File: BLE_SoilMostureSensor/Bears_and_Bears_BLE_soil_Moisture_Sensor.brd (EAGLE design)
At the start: 35.6 x 76.2 mm, 51 parts, among them Q1 2N3904, U2 EFR32BG13, X1 20317

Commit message: fixing antenna
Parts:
- removed FID1, FID2: FIDUCIAL"", microbuilder:FIDUCIAL_1MM
- removed TP6: TEST-POINT3, SparkFun-Connectors:PAD.03X.03
- added R11: 4.7k, SparkFun-Resistors:0603
- added Y1: (no value), Crystal_SMD_1.2x0.6:CRYSTAL_1.2X0.6
- L1: value L100 -> 33nH/±5%/500mA
- L2, L4: value 1.9NH -> 3.9NH
- U$3: value 38.4MHZ_CRYSTAL -> (none)
- moved U$3 88.2 mm to (12.5, 52.2), turned to 180 degrees
- moved U2 86.3 mm to (17.0, 56.5)
- moved TP4 85.6 mm to (8.26, 66.5)
- moved TP2 84.4 mm to (8.26, 68.4)
- moved TP5 77.7 mm to (22.5, 53.5)
- moved TP3 70.9 mm to (18.1, 51.0)
- moved R10 67.8 mm to (23.0, 51.8), turned to 180 degrees
- moved TP1 65.2 mm to (20.3, 47.3)
- moved R2 42.7 mm to (1.91, 48.3)
- moved FB1 38.7 mm to (8.57, 53.3)
- moved C11 34.3 mm to (8.57, 55.2), turned to 180 degrees
- moved L4 33.7 mm to (13.0, 69.1), turned to 180 degrees
- moved C12 32.8 mm to (8.57, 56.8), turned to 180 degrees
- moved C10 27.4 mm to (20.3, 69.2), turned to 180 degrees
- moved R9 27.0 mm to (16.2, 69.1), turned to 180 degrees
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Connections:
- removed net N$52: X1.9
- removed net N$7: TP6.P$1
- removed net N$8: TP5.P$1
- new net GND_DETECT: R11.1, U2.23, X1.9
- new net HFXTAL_N: U$3.1, U2.10
- new net HFXTAL_P: U$3.3, U2.11
- new net LFXTAL_N: U2.35, Y1.P$1
- new net LFXTAL_P: U2.36, Y1.P$2
- new net N$10: U2.6
- new net N$11: U2.7
- new net N$12: U2.8
- new net N$16: U2.26
- new net N$17: U2.27
- new net N$18: U2.28
- new net N$19: U2.29
- new net N$2: U2.14, U2.15, U2.37, U2.GND
- new net N$20: U2.30
- new net N$9: U2.5
- net DECOUPLE: now also U2.41; no longer U2.42
- net GND: now also U$3.GND, U$3.GND2, U2.16
- net IOP: now also U2.17
- net PAVDD: no longer FB2.1
- net RADIO_RESET: now also U2.12
- net RFVDD: now also U2.9
- net SCL: now also U2.47
- net SDA: now also U2.48
- net SENSOR_ENABLE: now also TP5.P$1, U2.24
- net SIG: now also U2.25
- net SOIL_MOIST_PWR: now also U2.20
- net TCK: now also U2.1
- net TDI: now also U2.4
- net TDO: now also U2.3
- net TMS: now also U2.2
- net VDCDC: no longer U2.41
- net VDD: now also FB2.1, R11.2; no longer C4.1, C5.1, C6.1, L1.1, U2.38, U2.39
- net VREGSW: now also U2.38
- net V_BATT: now also C4.1, C5.1, C6.1, L1.1, U2.39, U2.42
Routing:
- net V_BATT: track 0.00 -> 26.6 mm, vias 0 -> 2
- net N$3: track 0.00 -> 17.9 mm
- net PROBE1: track 0.00 -> 11.2 mm
- net VDCDC: track 0.00 -> 10.9 mm
- net SCL: track 0.00 -> 10.6 mm
- net SDA: track 0.00 -> 8.38 mm
- net TCK: track 0.00 -> 8.29 mm
- net VREGSW: track 0.00 -> 8.19 mm, vias 0 -> 2
- net AVDD: track 0.00 -> 7.01 mm
- net PAVDD: track 0.00 -> 6.60 mm
- net SDA_IN: track 0.00 -> 6.46 mm
- net RFVDD: track 0.00 -> 5.78 mm
- net SCL_IN: track 0.00 -> 4.02 mm
- net LFXTAL_N: track 0.00 -> 3.42 mm
- net LFXTAL_P: track 0.00 -> 3.37 mm
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- added copper zone on layer 1, net GND
- added copper zone on layer 16, net GND
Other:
- board size 35.6 x 76.2 mm -> 33.6 x 76.2 mm

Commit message: first prototype
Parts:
- removed STANDOFF1, STANDOFF2: STAND-OFF, SparkFun-Electromechanical:STAND-OFF
- added U$4: IMAGES#JPG, images#jpg(2):IMAGES#JPG
- E1: value ANTENNA-GROUNDEDTRACE-15.2MM -> ANTENNA-GROUNDEDTRACE-25.7MM; device SparkFun-RF:TRACE_ANTENNA_2.4GHZ_15.2MM -> SparkFun-RF:TRACE_ANTENNA_2.4GHZ_25.7MM
- moved FRAME2 107.9 mm to (59.1, -8.57)
- moved C6 62.5 mm to (64.4, 62.8), turned to 0 degrees
- moved R2 48.6 mm to (50.5, 47.3), turned to 0 degrees
- moved C9 44.8 mm to (56.2, 60.6), turned to 90 degrees
- moved U$2 43.2 mm to (45.4, 62.9)
- moved E1 40.8 mm to (53.3, 71.6)
- moved C2 40.7 mm to (70.0, 60.3)
- moved C3 40.7 mm to (70.0, 58.4)
- moved L1 40.7 mm to (70.0, 54.9)
- moved R7 40.7 mm to (70.0, 56.7)
- moved X1 40.4 mm to (43.0, 50.8)
- moved C12 40.3 mm to (48.9, 56.8)
- moved Y1 40.1 mm to (62.2, 56.4), turned to 90 degrees
- moved Q1 40.0 mm to (69.4, 49.2)
- moved R1 40.0 mm to (69.4, 52.1)
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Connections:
- removed net N$2: U2.14, U2.15, U2.37, U2.GND
- net GND: now also E1.GND2, U2.14, U2.15, U2.37, U2.GND
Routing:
- net VDD: track 2.45 -> 87.9 mm, vias 0 -> 4
- net PAVDD: track 6.60 -> 50.9 mm, vias 0 -> 2
- net SENSOR_ENABLE: track 0.00 -> 31.7 mm, vias 0 -> 2
- net V_BATT: track 26.6 -> 57.3 mm, vias 2 -> 7
- net GND_DETECT: track 0.00 -> 25.6 mm, vias 0 -> 2
- net AVDD: track 7.01 -> 29.4 mm, vias 0 -> 2
- net SOIL_MOIST_PWR: track 0.00 -> 20.9 mm
- net VDCDC: track 10.9 -> 30.3 mm, vias 0 -> 3
- net GND: track 0.00 -> 17.0 mm, vias 0 -> 17
- net PROBE2: track 0.00 -> 16.1 mm
- net RFVDD: track 5.78 -> 21.4 mm, vias 0 -> 3
- net SDA: track 8.38 -> 22.6 mm, vias 0 -> 2
- net SCL_IN: track 4.02 -> 18.1 mm, vias 0 -> 2
- net SIG: track 1.97 -> 14.2 mm
- net TDI: track 0.00 -> 10.3 mm, vias 0 -> 2
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- added copper zone on layer 2, net GND
- added copper zone on layer 15, net V_BATT
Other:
- board size 33.6 x 76.2 mm -> 33.6 x 78.4 mm
- board text added: "1"
- board text added: "2"
- board text added: "3"
- board text added: "4"
- board text added: "5"
- board text added: "BLE SOIL MOISTURE SENSOR"
- board text added: "LIGHT"
- board text added: "TEMP"

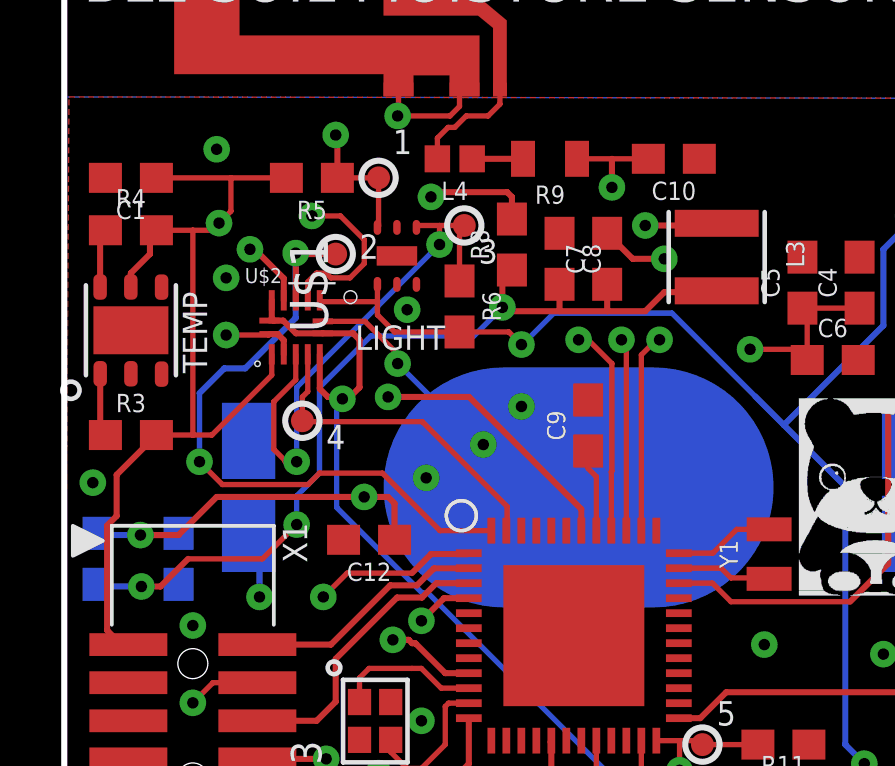
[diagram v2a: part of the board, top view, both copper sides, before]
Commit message: updating sch - 12c, power
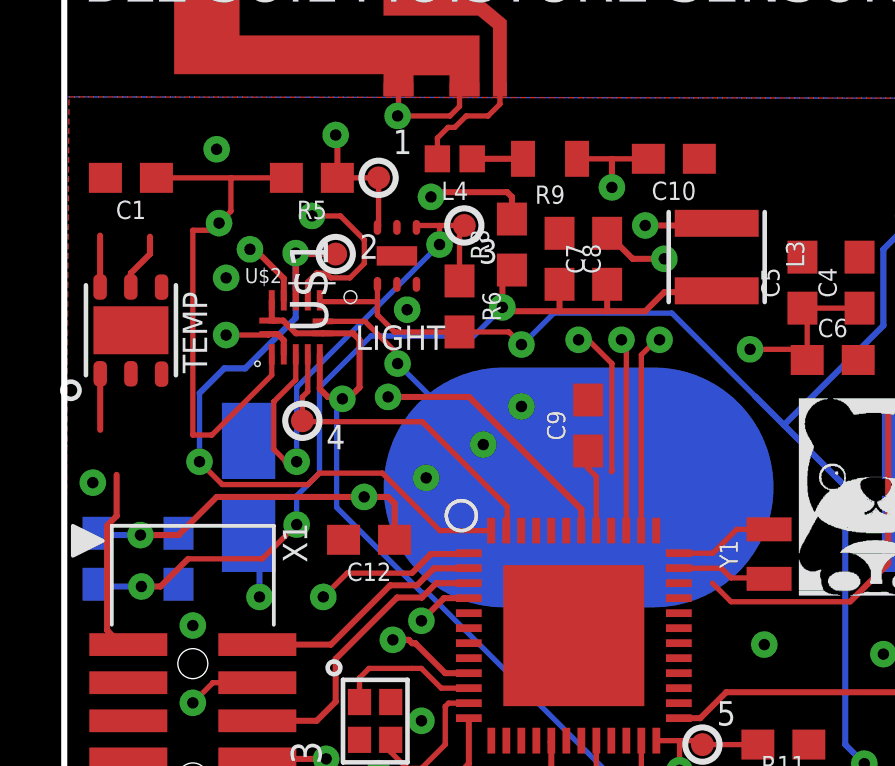
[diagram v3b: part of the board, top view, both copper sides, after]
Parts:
- removed R3, R4: 10k, SparkFun-Resistors:0603
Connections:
- removed net N$1: R4.1, U1.SCL
- removed net N$4: R3.1, U1.SDA
- new net DVDD: U2.40
- net AVDD: now also U2.34; no longer U2.40
- net PAVDD: now also U2.18; no longer U2.34
- net SCL_IN: now also U1.SCL
- net SDA_IN: now also U1.SDA
- net VDD: no longer R3.2, R4.2
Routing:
- net VDD: track 87.9 -> 83.2 mm
- net N$4: track 2.11 -> 0.00 mm
- net AVDD: track 29.4 -> 27.5 mm
- net N$1: track 1.97 -> 0.00 mm
- net SDA_IN: track 12.8 -> 14.6 mm
- net SCL_IN: track 18.1 -> 19.8 mm
- net PAVDD: track 50.9 -> 49.8 mm
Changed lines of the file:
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@@
 <attribute name="PROD_ID" value="CAP-00810" x="40.9575" y="68.8975" size="1.778" layer="27" rot="R180" display="off"/>
-</element>
-<element name="R3" library="SparkFun-Resistors" package="0603" value="10k" x="40.9575" y="60.325">
-<attribute name="PROD_ID" value="RES-00824" x="40.9575" y="60.325" size="1.778" layer="27" display="off"/>
-</element>
-<element name="R4" library="SparkFun-Resistors" package="0603" value="10k" x="40.9575" y="67.15125">
-<attribute name="PROD_ID" value="RES-00824" x="40.9575" y="67.15125" size="1.778" layer="27" display="off"/>
 </element>
 <element name="U$1" library="ALS_OPT3001" package="6PIN_USON" value="" x="50.8" y="65.24625" rot="R90"/>
@@
 <wire x1="41.275" y1="45.4025" x2="41.275" y2="38.4175" width="0.1778" layer="1"/>
 </signal>
-<signal name="N$1">
-<contactref element="U1" pad="SCL"/>
-<contactref element="R4" pad="1"/>
-<wire x1="39.9305" y1="65.2595" x2="39.9305" y2="66.97425" width="0.2032" layer="1"/>
-<wire x1="39.9305" y1="66.97425" x2="40.1075" y2="67.15125" width="0.2032" layer="1"/>
-</signal>
-<signal name="N$4">
-<contactref element="U1" pad="SDA"/>
-<contactref element="R3" pad="1"/>
-<wire x1="39.9335" y1="62.3675" x2="39.9335" y2="60.499" width="0.2032" layer="1"/>
-<wire x1="39.9335" y1="60.499" x2="40.1075" y2="60.325" width="0.2032" layer="1"/>
-</signal>
 <signal name="SCL_IN">
 <contactref element="U$2" pad="NO2"/>
@@
 <via x="46.482" y="59.436" extent="1-16" drill="0.381"/>
 <via x="51.2445" y="66.675" extent="1-16" drill="0.381"/>
+<contactref element="U1" pad="SCL"/>
+<wire x1="39.9305" y1="65.2595" x2="39.9305" y2="66.97425" width="0.2032" layer="1"/>
+<wire x1="39.9305" y1="65.2595" x2="46.4525" y2="63.015" width="0" layer="19" extent="1-1"/>
 </signal>
 <signal name="SCL">
@@
 <contactref element="U$2" pad="NO3"/>
 <contactref element="C1" pad="1"/>
-<contactref element="R3" pad="2"/>
-<contactref element="R4" pad="2"/>
 <contactref element="U1" pad="VCC"/>
 <contactref element="U$1" pad="1"/>
@@
 <wire x1="40.9545" y1="65.2615" x2="40.9545" y2="65.7195" width="0.2032" layer="1"/>
 <wire x1="41.5925" y1="66.3575" x2="40.9545" y2="65.7195" width="0.2032" layer="1"/>
-<wire x1="41.8075" y1="67.15125" x2="41.5925" y2="66.93625" width="0.2032" layer="1"/>
 <wire x1="41.5925" y1="66.93625" x2="41.5925" y2="66.3575" width="0.2032" layer="1"/>
 <wire x1="41.8075" y1="68.8975" x2="44.29125" y2="68.8975" width="0.1778" layer="1"/>
 <wire x1="44.29125" y1="68.8975" x2="46.14" y2="68.8975" width="0.1778" layer="1"/>
-<wire x1="41.8075" y1="67.15125" x2="43.02125" y2="67.15125" width="0.1778" layer="1"/>
 <wire x1="43.02125" y1="67.15125" x2="43.65625" y2="67.15125" width="0.1778" layer="1"/>
 <wire x1="44.29125" y1="67.78625" x2="44.29125" y2="68.8975" width="0.1778" layer="1"/>
@@
 <wire x1="45.6525" y1="62.32125" x2="43.65625" y2="60.325" width="0.1778" layer="1"/>
 <wire x1="43.65625" y1="60.325" x2="43.02125" y2="60.325" width="0.1778" layer="1"/>
-<wire x1="43.02125" y1="60.325" x2="41.8075" y2="60.325" width="0.1778" layer="1"/>
 <wire x1="43.02125" y1="67.15125" x2="43.02125" y2="60.325" width="0.1778" layer="1"/>
-<wire x1="41.8075" y1="60.325" x2="41.75125" y2="60.26875" width="0.1778" layer="1"/>
 <wire x1="40.64" y1="53.34" x2="40.87125" y2="53.34" width="0.1778" layer="1"/>
 <wire x1="58.9915" y1="64.389" x2="61.769625" y2="61.610875" width="0.1778" layer="16"/>
@@
 <wire x1="66.04" y1="63.97625" x2="62.722125" y2="60.658375" width="0.2032" layer="16"/>
 <wire x1="66.04" y1="66.51625" x2="66.04" y2="63.97625" width="0.2032" layer="16"/>
-<wire x1="41.8075" y1="60.325" x2="40.48125" y2="58.99875" width="0.2032" layer="1"/>
 <wire x1="40.48125" y1="57.62625" x2="40.16375" y2="57.30875" width="0.2032" layer="1"/>
 <wire x1="40.16375" y1="57.30875" x2="40.16375" y2="53.81625" width="0.2032" layer="1"/>
@@
 <wire x1="53.975" y1="63.34125" x2="54.00675" y2="63.34125" width="0.1778" layer="16"/>
 <wire x1="54.00675" y1="63.34125" x2="55.0545" y2="64.389" width="0.1778" layer="16"/>
+<wire x1="43.02125" y1="67.15125" x2="41.5925" y2="66.93625" width="0" layer="19" extent="1-1"/>
+<wire x1="40.48125" y1="58.99875" x2="43.02125" y2="60.325" width="0" layer="19" extent="1-1"/>
 </signal>
 <signal name="SDA_IN">
@@
 <wire x1="47.84" y1="68.8975" x2="47.84" y2="70.27" width="0.2032" layer="1"/>
 <wire x1="47.84" y1="70.27" x2="47.78375" y2="70.32625" width="0.2032" layer="1"/>
+<contactref element="U1" pad="SDA"/>
+<wire x1="39.9335" y1="62.3675" x2="39.9335" y2="60.499" width="0.2032" layer="1"/>
+<wire x1="39.9335" y1="62.3675" x2="44.92625" y2="66.51625" width="0" layer="19" extent="1-1"/>
 </signal>
 <signal name="SDA">
@@
 <contactref element="C3" pad="1"/>
 <contactref element="C2" pad="2"/>
-<contactref element="U2" pad="40"/>
 <wire x1="69.15875" y1="56.67375" x2="68.10375" y2="56.67375" width="0.1778" layer="1"/>
 <wire x1="68.10375" y1="56.67375" x2="67.945" y2="56.8325" width="0.1778" layer="1"/>
@@
 <wire x1="67.945" y1="58.42" x2="67.945" y2="60.0075" width="0.1778" layer="1"/>
 <wire x1="69.15875" y1="58.42" x2="67.945" y2="58.42" width="0.1778" layer="1"/>
-<wire x1="56.97125" y1="57.1375" x2="56.97125" y2="59.10315625" width="0.1778" layer="1"/>
 <wire x1="56.97125" y1="59.10315625" x2="56.9896" y2="59.12150625" width="0.1778" layer="1"/>
 <wire x1="56.9896" y1="59.12150625" x2="56.9896" y2="62.7079" width="0.1778" layer="1"/>
@@
 <wire x1="57.94375" y1="61.43625" x2="68.8975" y2="61.43625" width="0.1778" layer="2"/>
 <wire x1="68.8975" y1="61.43625" x2="69.05625" y2="61.595" width="0.1778" layer="2"/>
+<contactref element="U2" pad="34"/>
+<wire x1="59.22125" y1="55.3875" x2="56.97125" y2="59.10315625" width="0" layer="19" extent="1-1"/>
 </signal>
 <signal name="VDCDC">
@@
 <contactref element="C13" pad="1"/>
 <contactref element="C14" pad="1"/>
-<contactref element="U2" pad="34"/>
 <wire x1="66.9925" y1="63.8175" x2="67.31" y2="63.5" width="0.2032" layer="1"/>
 <wire x1="70.485" y1="63.5" x2="68.8975" y2="63.5" width="0.2032" layer="1"/>
@@
 <wire x1="68.8975" y1="64.555" x2="68.8975" y2="63.5" width="0.2032" layer="1"/>
 <wire x1="66.9925" y1="64.555" x2="66.9925" y2="63.8175" width="0.2032" layer="1"/>
-<wire x1="59.22125" y1="55.3875" x2="60.34125" y2="55.3875" width="0.1778" layer="1"/>
 <wire x1="60.34125" y1="55.3875" x2="60.96" y2="54.76875" width="0.1778" layer="1"/>
 <wire x1="60.96" y1="54.76875" x2="64.92875" y2="54.76875" width="0.1778" layer="1"/>
@@
 <wire x1="66.19875" y1="61.11875" x2="67.78625" y2="62.70625" width="0.2032" layer="1"/>
 <wire x1="66.19875" y1="56.03875" x2="66.19875" y2="61.11875" width="0.2032" layer="1"/>
+<contactref element="U2" pad="18"/>
+<wire x1="55.47125" y1="50.1375" x2="60.34125" y2="55.3875" width="0" layer="19" extent="1-1"/>
 </signal>
 <signal name="N$3">
@@
 <wire x1="60.35625" y1="56.3875" x2="61.15" y2="57.18125" width="0.1778" layer="1"/>
 </signal>
+<signal name="DVDD">
+<contactref element="U2" pad="40"/>
+</signal>
 </signals>

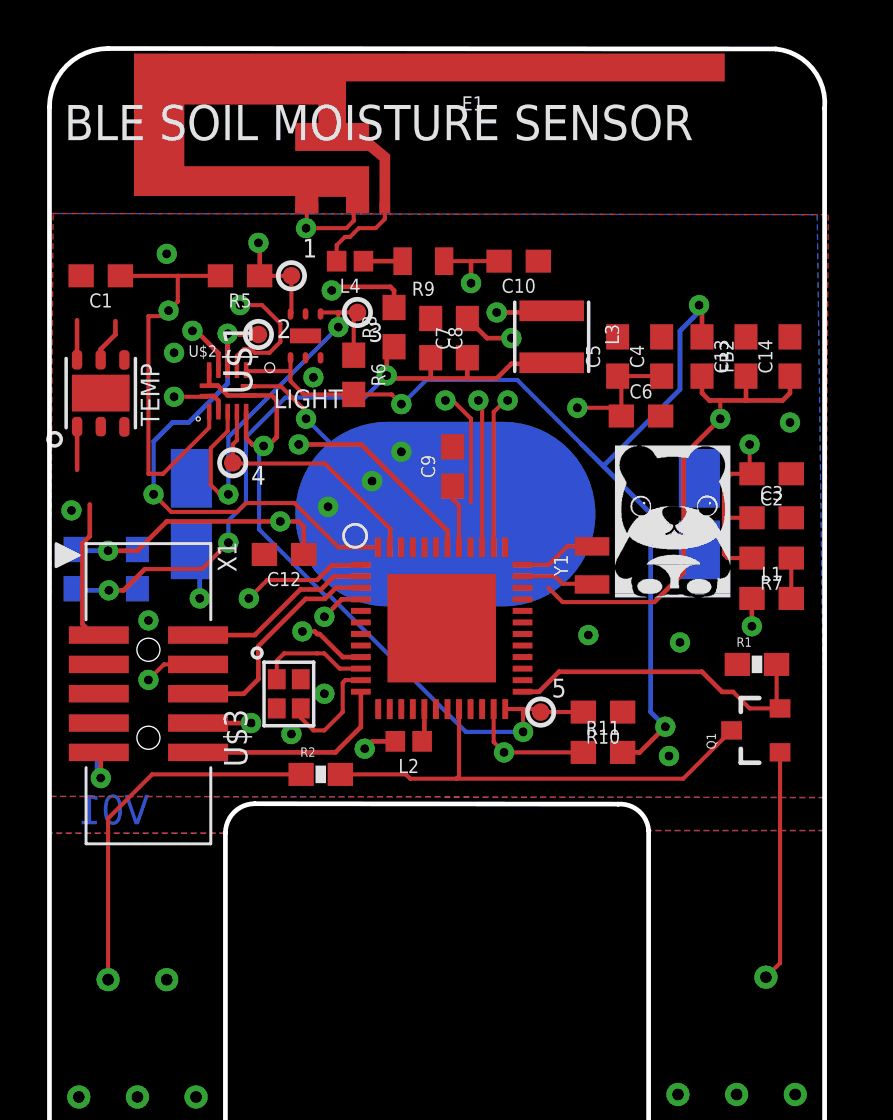
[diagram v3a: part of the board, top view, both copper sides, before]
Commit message: Make required changes:
- Rotate temp sensor and reroute
- Route AVDD to MCU
- Route PAVDD to MCU
- Change SWD jack to POGO type
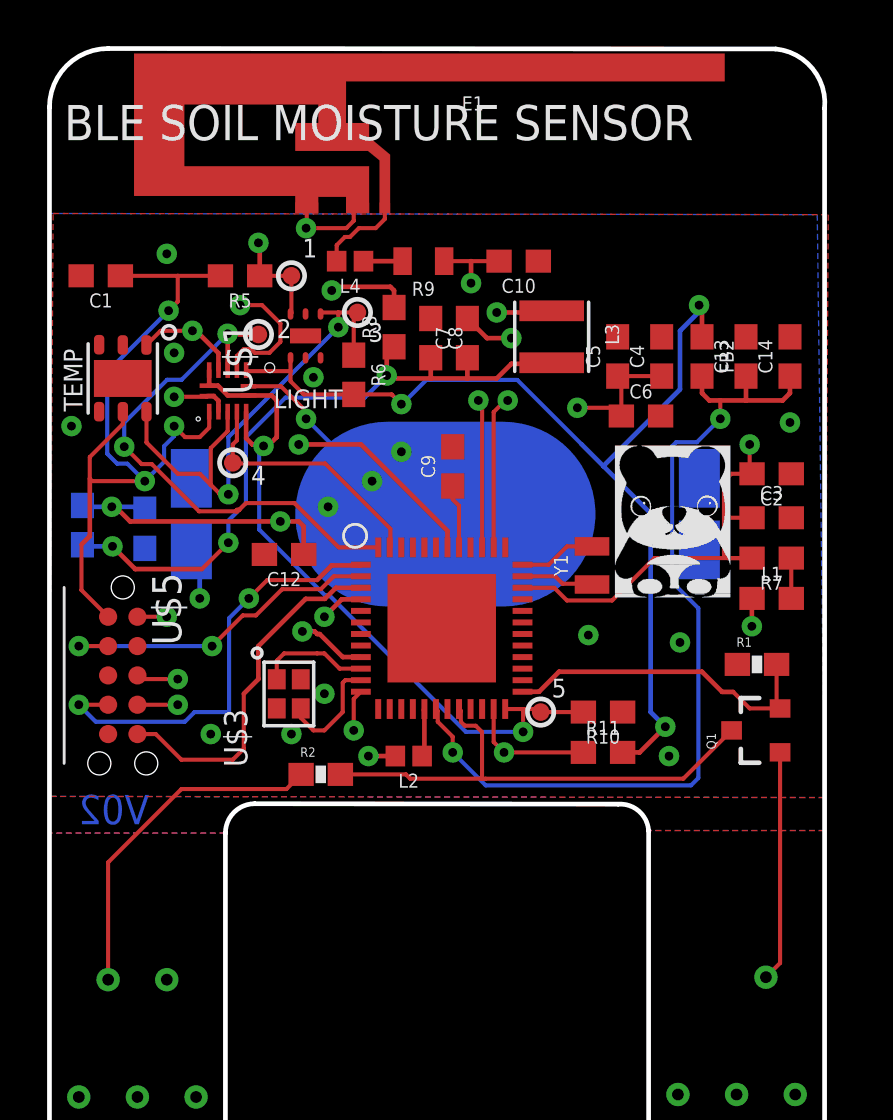
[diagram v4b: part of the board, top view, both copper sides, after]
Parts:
- removed X1: 20317, microbuilder:2X05_1.27MM_BOX_POSTS
- added U$5: TC2050-MCP-NL, TC2050:TC2030-MCP-NL
- moved FB1 1.93 mm to (40.2, 58.1)
- moved C11 1.77 mm to (42.9, 57.9)
- moved U1 1.14 mm to (41.9, 64.5), turned to 270 degrees
- moved L2 0.63 mm to (54.3, 48.1)
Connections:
- net GND: now also U$5.3, U$5.5; no longer X1.3, X1.5
- net GND_DETECT: now also U$5.7; no longer X1.9
- net RADIO_RESET: now also U$5.10; no longer X1.10
- net TCK: now also U$5.4; no longer X1.4
- net TDI: now also U$5.8; no longer X1.8
- net TDO: now also U$5.6; no longer X1.6
- net TMS: now also U$5.2; no longer X1.2
- net VDD: now also U$5.1; no longer X1.1
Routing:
- net PAVDD: track 49.8 -> 66.8 mm, vias 2 -> 3
- net AVDD: track 27.5 -> 19.5 mm, vias 2 -> 1
- net VDD: track 83.2 -> 90.5 mm, vias 4 -> 6
- net TMS: track 8.11 -> 14.9 mm, vias 0 -> 2
- net TDO: track 9.79 -> 15.5 mm
- net TCK: track 14.5 -> 19.0 mm
- net RADIO_RESET: track 9.03 -> 13.4 mm, vias 0 -> 2
- net GND_DETECT: track 25.6 -> 22.2 mm
- net SCL_IN: track 19.8 -> 23.0 mm
- net TDI: track 10.3 -> 12.1 mm
- net PROBE2: track 16.1 -> 15.0 mm
- net SDA: track 22.6 -> 23.3 mm
- net SOIL_MOIST_PWR: track 20.9 -> 21.6 mm
- net IOP: track 1.50 -> 2.14 mm
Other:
- board text added: "V02"
- board text removed: "V01"
